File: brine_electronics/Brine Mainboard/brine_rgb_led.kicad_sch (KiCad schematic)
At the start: 3 parts

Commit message: Updated electronics/enclosure designs
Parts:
- removed D1: WS2812B, LED_SMD:LED_WS2812B_PLCC4_5.0x5.0mm_P3.2mm, symbol LED:WS2812B
- added D2: SK6812, LED_SMD:LED_SK6812_PLCC4_5.0x5.0mm_P3.2mm, symbol LED:SK6812
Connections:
- net +5V: now also D2.3 (VDD)
- net GND: now also D2.1 (VSS)
- net at R4.1: now also D2.2 (DIN)
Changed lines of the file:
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@@
-	)
-	(symbol
-		(lib_id "LED:WS2812B")
-		(at 127 88.9 0)
-		(unit 1)
-		(exclude_from_sim no)
-		(in_bom yes)
-		(on_board yes)
-		(dnp no)
-		(fields_autoplaced yes)
-		(property "Reference" "D1"
-			(at 138.43 82.4798 0)
-			(effects
-				(font
-					(size 1.27 1.27)
-				)
-			)
-		)
-		(property "Value" "WS2812B"
-			(at 138.43 85.0198 0)
-			(effects
-				(font
-					(size 1.27 1.27)
-				)
-			)
-		)
-		(property "Footprint" "LED_SMD:LED_WS2812B_PLCC4_5.0x5.0mm_P3.2mm"
-			(at 128.27 96.52 0)
-			(effects
-				(font
-					(size 1.27 1.27)
-				)
-				(justify left top)
-				(hide yes)
-			)
-		)
-		(property "Datasheet" "https://cdn-shop.adafruit.com/datasheets/WS2812B.pdf"
-			(at 129.54 98.425 0)
-			(effects
-				(font
-					(size 1.27 1.27)
-				)
-				(justify left top)
-				(hide yes)
-			)
-		)
-		(property "Description" "RGB LED with integrated controller"
-			(at 127 88.9 0)
-			(effects
-				(font
-					(size 1.27 1.27)
-				)
-				(hide yes)
-			)
-		)
-		(pin "4"
-		)
-		(pin "2"
-		)
-		(pin "3"
-		)
-		(pin "1"
-		)
-		(instances
-			(project "Brine"
-				(path "/da3a4ef2-0e38-46f1-a1fc-55d8e0a83a54/6d2918a7-c70e-4d9e-bb5b-f7d45fd4d68d"
-					(reference "D1")
-					(unit 1)
-				)
-			)
-		)
 	)
 	(symbol
@@
 					(unit 1)
 				)
+			)
+		)
+	)
+	(symbol
+		(lib_id "LED:SK6812")
+		(at 127 88.9 0)
+		(unit 1)
+		(exclude_from_sim no)
+		(in_bom yes)
+		(on_board yes)
+		(dnp no)
+		(fields_autoplaced yes)
+		(property "Reference" "D2"
+			(at 137.16 82.4798 0)
+			(effects
+				(font
+					(size 1.27 1.27)
+				)
+			)
+		)
+		(property "Value" "SK6812"
+			(at 137.16 85.0198 0)
+			(effects
+				(font
+					(size 1.27 1.27)
+				)
+			)
+		)
+		(property "Footprint" "LED_SMD:LED_SK6812_PLCC4_5.0x5.0mm_P3.2mm"
+			(at 128.27 96.52 0)
+			(effects
+				(font
+					(size 1.27 1.27)
+				)
+				(justify left top)
+				(hide yes)
+			)
+		)
+		(property "Datasheet" "https://cdn-shop.adafruit.com/product-files/1138/SK6812+LED+datasheet+.pdf"
+			(at 129.54 98.425 0)
+			(effects
+				(font
+					(size 1.27 1.27)
+				)
+				(justify left top)
+				(hide yes)
+			)
+		)
+		(property "Description" "RGB LED with integrated controller"
+			(at 127 88.9 0)
+			(effects
+				(font
+					(size 1.27 1.27)
+				)
+				(hide yes)
+			)
+		)
+		(pin "2"
+		)
+		(pin "3"
+		)
+		(pin "4"
+		)
+		(pin "1"
+		)
+		(instances
+			(project ""
+				(path "/da3a4ef2-0e38-46f1-a1fc-55d8e0a83a54/6d2918a7-c70e-4d9e-bb5b-f7d45fd4d68d"
+					(reference "D2")
+					(unit 1)
+				)

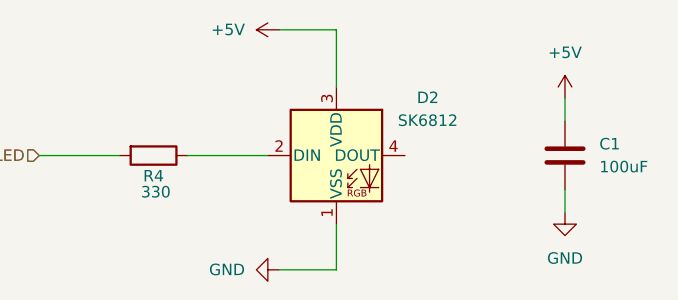
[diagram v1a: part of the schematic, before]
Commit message: Implemented power latch circuit ⚡
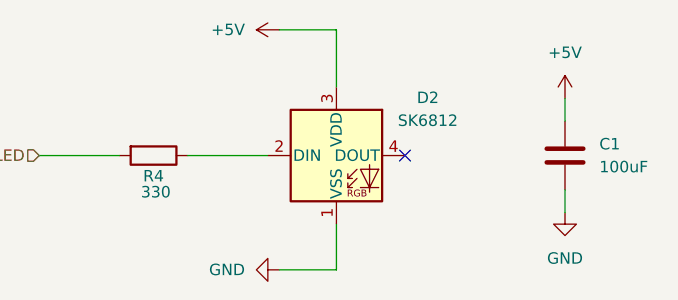
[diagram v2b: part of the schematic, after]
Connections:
- no-connect marks 0 -> 1
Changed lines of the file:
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@@
 		(comment 3 "It can also be used during debugging for various purposes.")
+	)
+	(no_connect
+		(at 134.62 88.9)
 	)
 	(wire

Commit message: Updated PCB manufacturing files :mechanical_arm:
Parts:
- added C5: 100uF, Capacitor_SMD:C_0805_2012Metric, symbol Device:C
- added U4: 74AHCT1G125, Package_TO_SOT_SMD:SOT-23-5, symbol 74xGxx:74AHCT1G125
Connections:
- net +5V: now also C5.1, U4.5 (VCC)
- net GND: now also C5.2, U4.1, U4.3 (GND)
- net LED: now also U4.2; no longer R4.2
- new net: R4.2, U4.4

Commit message: Updated production files 🏭
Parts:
- C1, C5: LCSC Part # (none) -> C141660
- D2: LCSC Part # (none) -> C5378720
- R4: LCSC Part # (none) -> C212379
- U4: LCSC Part # (none) -> C52140417
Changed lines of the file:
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@@
+			)
+		)
+		(property "Color" ""
+			(at 106.68 88.9 90)
+			(hide yes)
+			(show_name no)
+			(do_not_autoplace no)
+			(effects
+				(font
+					(size 1.27 1.27)
+				)
+			)
+		)
+		(property "LCSC Part #" "C212379"
+			(at 106.68 88.9 90)
+			(hide yes)
+			(show_name no)
+			(do_not_autoplace no)
+			(effects
+				(font
+					(size 1.27 1.27)
+				)
 			)
 		)
@@
 			)
 		)
+		(property "Color" ""
+			(at 44.45 88.9 0)
+			(hide yes)
+			(show_name no)
+			(do_not_autoplace no)
+			(effects
+				(font
+					(size 1.27 1.27)
+				)
+			)
+		)
+		(property "LCSC Part #" "C141660"
+			(at 44.45 88.9 0)
+			(hide yes)
+			(show_name no)
+			(do_not_autoplace no)
+			(effects
+				(font
+					(size 1.27 1.27)
+				)
+			)
+		)
 		(pin "2"
 		)
@@
 			)
 		)
+		(property "Color" ""
+			(at 127 88.9 0)
+			(hide yes)
+			(show_name no)
+			(do_not_autoplace no)
+			(effects
+				(font
+					(size 1.27 1.27)
+				)
+			)
+		)
+		(property "LCSC Part #" "C5378720"
+			(at 127 88.9 0)
+			(hide yes)
+			(show_name no)
+			(do_not_autoplace no)
+			(effects
+				(font
+					(size 1.27 1.27)
+				)
+			)
+		)
 		(pin "2"
 		)
@@
 		)
 		(property "Footprint" "Package_TO_SOT_SMD:SOT-23-5"
-			(at 83.82 88.9 0)
+			(at 80.264 109.22 0)
 			(show_name no)
 			(do_not_autoplace no)
@@
 		)
 		(property "Description" "Single Buffer Gate Tri-State, Low-Voltage CMOS"
+			(at 83.82 88.9 0)
+			(hide yes)
+			(show_name no)
+			(do_not_autoplace no)
+			(effects
+				(font
+					(size 1.27 1.27)
+				)
+			)
+		)
+		(property "Color" ""
+			(at 83.82 88.9 0)
+			(hide yes)
+			(show_name no)
+			(do_not_autoplace no)
+			(effects
+				(font
+					(size 1.27 1.27)
+				)
+			)
+		)
+		(property "LCSC Part #" "C52140417"
 			(at 83.82 88.9 0)
 			(hide yes)
@@
 			(at 152.4 88.9 0)
 			(hide yes)
+			(show_name no)
+			(do_not_autoplace no)
+			(effects
+				(font
+					(size 1.27 1.27)
+				)
+			)
+		)
+		(property "Color" ""
+			(at 152.4 88.9 0)
+			(hide yes)
+			(show_name no)
+			(do_not_autoplace no)
+			(effects
+				(font
+					(size 1.27 1.27)
+				)
+			)
+		)
+		(property "LCSC Part #" "C141660"
+			(at 152.4 88.9 0)
+			(hide yes)

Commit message: Updated electronics production files 🏭
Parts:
- C1, C5: JLCPCB Part # (none) -> C141660; LCSC Part # C141660 -> (none)
- D2: JLCPCB Part # (none) -> C5378720; LCSC Part # C5378720 -> (none)
- R4: JLCPCB Part # (none) -> C212379; LCSC Part # C212379 -> (none)
- U4: JLCPCB Part # (none) -> C52140417; LCSC Part # C52140417 -> (none)
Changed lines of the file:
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@@
 			)
 		)
-		(property "LCSC Part #" "C212379"
+		(property "JLCPCB Part #" "C212379"
 			(at 106.68 88.9 90)
 			(hide yes)
@@
 			)
 		)
-		(property "LCSC Part #" "C141660"
+		(property "JLCPCB Part #" "C141660"
 			(at 44.45 88.9 0)
 			(hide yes)
@@
 			)
 		)
-		(property "LCSC Part #" "C5378720"
+		(property "JLCPCB Part #" "C5378720"
 			(at 127 88.9 0)
 			(hide yes)
@@
 			)
 		)
-		(property "LCSC Part #" "C52140417"
+		(property "JLCPCB Part #" "C52140417"
 			(at 83.82 88.9 0)
 			(hide yes)
@@
 			)
 		)
-		(property "LCSC Part #" "C141660"
+		(property "JLCPCB Part #" "C141660"
 			(at 152.4 88.9 0)
 			(hide yes)
